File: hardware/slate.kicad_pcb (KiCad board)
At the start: 4 copper layers, 2 parts, among them U1 A33, U2 H5TQ4G63EFR

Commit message: Update
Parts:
- added R1: 240, Resistor_SMD:R_0201_0603Metric, B.Cu at (156.8, 103.5)
- added R2: 240, Resistor_SMD:R_0201_0603Metric, F.Cu at (171.4, 93.7)
- added U3: H5TQ4G63EFR, Package_BGA:FBGA-96_7.5x13mm_Layout9x16_P0.8mm, F.Cu at (159.1, 119.4)
- U2: moved to B.Cu
- moved U1 17.7 mm to (137.1, 101.5)
- moved U2 12.1 mm to (169.0, 119.5), turned to 180 degrees
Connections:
- U1 pad H5: VCC-DRAM -> +1V5
- U1 pad H6: VCC-DRAM -> +1V5
- U1 pad J5: VCC-DRAM -> +1V5
- U1 pad J6: VCC-DRAM -> +1V5
- U1 pad K5: VCC-DRAM -> +1V5
- U1 pad L5: VCC-DRAM -> +1V5
- U2 pad A1: VDDQ -> +1V5
- U2 pad A8: VDDQ -> +1V5
- U2 pad B2: VDD -> +1V5
- U2 pad C1: VDDQ -> +1V5
- U2 pad C9: VDDQ -> +1V5
- U2 pad D2: VDDQ -> +1V5
- U2 pad D9: VDD -> +1V5
- U2 pad E9: VDDQ -> +1V5
- U2 pad F1: VDDQ -> +1V5
- U2 pad G7: VDD -> +1V5
- U2 pad H2: VDDQ -> +1V5
- U2 pad H9: VDDQ -> +1V5
- U2 pad J3: unconnected-(U2-~{RAS}-PadJ3) -> /DDR3 RAM/~{RAS}
- U2 pad K2: VDD -> +1V5
- U2 pad K3: unconnected-(U2-~{CAS}-PadK3) -> /DDR3 RAM/~{CAS}
- U2 pad K8: VDD -> +1V5
- U2 pad L2: unconnected-(U2-~{CS}-PadL2) -> /DDR3 RAM/~{DDRCS}
- U2 pad L3: unconnected-(U2-~{WE}-PadL3) -> /DDR3 RAM/~{WE}
- U2 pad L7: unconnected-(U2-A10/AP-PadL7) -> /DDR3 RAM/A10
- U2 pad L8: unconnected-(U2-ZQ-PadL8) -> Net-(U2-ZQ)
- U2 pad M2: unconnected-(U2-BA0-PadM2) -> /DDR3 RAM/BA0
- U2 pad M3: unconnected-(U2-BA2-PadM3) -> /DDR3 RAM/BA2
- U2 pad N1: VDD -> +1V5
- U2 pad N2: unconnected-(U2-A3-PadN2) -> /DDR3 RAM/A3
- U2 pad N3: unconnected-(U2-A0-PadN3) -> /DDR3 RAM/A0
- U2 pad N7: unconnected-(U2-A12/~{BC}-PadN7) -> /DDR3 RAM/A12
- U2 pad N8: unconnected-(U2-BA1-PadN8) -> /DDR3 RAM/BA1
- U2 pad N9: VDD -> +1V5
- U2 pad P2: unconnected-(U2-A5-PadP2) -> /DDR3 RAM/A5
- U2 pad P3: unconnected-(U2-A2-PadP3) -> /DDR3 RAM/A2
- U2 pad P7: unconnected-(U2-A1-PadP7) -> /DDR3 RAM/A1
- U2 pad P8: unconnected-(U2-A4-PadP8) -> /DDR3 RAM/A4
- U2 pad R1: VDD -> +1V5
- U2 pad R2: unconnected-(U2-A7-PadR2) -> /DDR3 RAM/A7
- U2 pad R3: unconnected-(U2-A9-PadR3) -> /DDR3 RAM/A9
- U2 pad R7: unconnected-(U2-A11-PadR7) -> /DDR3 RAM/A11
- U2 pad R8: unconnected-(U2-A6-PadR8) -> /DDR3 RAM/A6
- U2 pad R9: VDD -> +1V5
- U2 pad T2: unconnected-(U2-~{RESET}-PadT2) -> /DDR3 RAM/~{DDRRST}
- U2 pad T3: unconnected-(U2-A13-PadT3) -> /DDR3 RAM/A13
- U2 pad T7: unconnected-(U2-A14-PadT7) -> /DDR3 RAM/A14
- U2 pad T8: unconnected-(U2-A8-PadT8) -> /DDR3 RAM/A8

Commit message: Update
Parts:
- added C1: 100n, Capacitor_SMD:C_0201_0603Metric, F.Cu at (141.3, 43.2)
- added C10: 100n, Capacitor_SMD:C_0201_0603Metric, F.Cu at (143.7, 45.0)
- added C11: 100n, Capacitor_SMD:C_0201_0603Metric, F.Cu at (143.7, 46.7)
- added C12: 100n, Capacitor_SMD:C_0201_0603Metric, F.Cu at (143.7, 48.5)
- added C13: 100n, Capacitor_SMD:C_0201_0603Metric, F.Cu at (143.7, 50.2)
- added C14: 100n, Capacitor_SMD:C_0201_0603Metric, F.Cu at (143.7, 52.0)
- added C15: 100n, Capacitor_SMD:C_0201_0603Metric, F.Cu at (143.7, 53.7)
- added C16: 100n, Capacitor_SMD:C_0201_0603Metric, F.Cu at (143.7, 55.5)
- added C17: 100n, Capacitor_SMD:C_0201_0603Metric, F.Cu at (146.2, 43.2)
- added C18: 100n, Capacitor_SMD:C_0201_0603Metric, F.Cu at (146.2, 45.0)
- added C19: 100n, Capacitor_SMD:C_0201_0603Metric, F.Cu at (146.2, 46.7)
- added C2: 100n, Capacitor_SMD:C_0201_0603Metric, F.Cu at (141.3, 45.0)
- added C20: 100n, Capacitor_SMD:C_0201_0603Metric, F.Cu at (146.2, 48.5)
- added C21: 100n, Capacitor_SMD:C_0201_0603Metric, F.Cu at (146.2, 50.2)
- added C22: 100n, Capacitor_SMD:C_0201_0603Metric, F.Cu at (146.2, 52.0)
- added C23: 100n, Capacitor_SMD:C_0201_0603Metric, F.Cu at (146.2, 53.7)
- added C24: 100n, Capacitor_SMD:C_0201_0603Metric, F.Cu at (146.2, 55.5)
- added C25: 100n, Capacitor_SMD:C_0201_0603Metric, F.Cu at (126.5, 98.8)
- added C26: 100n, Capacitor_SMD:C_0201_0603Metric, F.Cu at (126.5, 100.5)
- added C3: 100n, Capacitor_SMD:C_0201_0603Metric, F.Cu at (141.3, 46.7)
- added C4: 100n, Capacitor_SMD:C_0201_0603Metric, F.Cu at (141.3, 48.5)
- added C5: 100n, Capacitor_SMD:C_0201_0603Metric, F.Cu at (141.3, 50.2)
- added C6: 100n, Capacitor_SMD:C_0201_0603Metric, F.Cu at (141.3, 52.0)
- added C7: 100n, Capacitor_SMD:C_0201_0603Metric, F.Cu at (141.3, 53.7)
- added C8: 100n, Capacitor_SMD:C_0201_0603Metric, F.Cu at (141.3, 55.5)
- added C9: 100n, Capacitor_SMD:C_0201_0603Metric, F.Cu at (143.7, 43.2)
- added R10: 1k, Resistor_SMD:R_0201_0603Metric, F.Cu at (126.5, 104.0)
- added R3: 1k, Resistor_SMD:R_0201_0603Metric, F.Cu at (148.6, 45.0)
- added R4: 240, Resistor_SMD:R_0201_0603Metric, F.Cu at (131.3, 35.9)
- added R5: 2k, Resistor_SMD:R_0201_0603Metric, F.Cu at (148.6, 48.5)
- added R6: 240, Resistor_SMD:R_0201_0603Metric, F.Cu at (135.7, 35.9)
- added R7: 240, Resistor_SMD:R_0201_0603Metric, F.Cu at (131.3, 37.7)
- added R8: 240, Resistor_SMD:R_0201_0603Metric, F.Cu at (131.3, 39.4)
- added R9: 1k, Resistor_SMD:R_0201_0603Metric, F.Cu at (126.5, 102.3)
- R2: value 240 -> 1k
- U2: value H5TQ4G63EFR -> H5TQ4G83EFR; footprint Package_BGA:FBGA-96_7.5x13mm_Layout9x16_P0.8mm -> Package_BGA:FBGA-78_7.5x11mm_Layout2x3x13_P0.8mm; moved to F.Cu
- U3: value H5TQ4G63EFR -> H5TQ4G83EFR; footprint Package_BGA:FBGA-96_7.5x13mm_Layout9x16_P0.8mm -> Package_BGA:FBGA-78_7.5x11mm_Layout2x3x13_P0.8mm
- moved U2 83.7 mm to (119.6, 51.9), turned to 0 degrees
- moved U3 72.5 mm to (132.6, 51.9)
- moved R1 67.3 mm to (137.8, 38.9)
- moved R2 55.4 mm to (148.6, 43.2)
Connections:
- R1 pad 1: Net-(U2-ZQ) -> Net-(U2-ZQ0)
- R2 pad 1: Net-(U3-ZQ) -> +1V5
- R2 pad 2: GND -> Net-(U2-VREFCA)
- U1 pad A1: unconnected-(U1B-DA6-PadA1) -> /A33/A6
- U1 pad B1: unconnected-(U1B-DA8-PadB1) -> /A33/A8
- U1 pad C1: unconnected-(U1B-DA14-PadC1) -> /A33/A14
- U1 pad C2: unconnected-(U1B-DA11-PadC2) -> /A33/A11
- U1 pad D1: unconnected-(U1B-DA1-PadD1) -> /A33/A1
- U1 pad D2: unconnected-(U1B-DA4-PadD2) -> /A33/A4
- U1 pad E1: unconnected-(U1B-DA12-PadE1) -> /A33/A12
- U1 pad E2: unconnected-(U1B-DA10-PadE2) -> /A33/A10
- U1 pad E3: unconnected-(U1B-DA15-PadE3) -> /A33/A15
- U1 pad E4: unconnected-(U1B-DA0-PadE4) -> /A33/A0
- U1 pad F1: unconnected-(U1B-DA5-PadF1) -> /A33/A5
- U1 pad F2: unconnected-(U1B-DA2-PadF2) -> /A33/A2
- U1 pad F3: unconnected-(U1B-DA13-PadF3) -> /A33/A13
- U1 pad F4: unconnected-(U1B-DA9-PadF4) -> /A33/A9
- U1 pad G1: unconnected-(U1B-DCK-PadG1) -> /A33/CLK+
- U1 pad G2: unconnected-(U1B-DCKB-PadG2) -> /A33/CLK-
- U1 pad G3: unconnected-(U1B-DRST-PadG3) -> /A33/~{RESET}
- U1 pad G4: unconnected-(U1B-DA7-PadG4) -> /A33/A7
- U1 pad H3: unconnected-(U1B-DA3-PadH3) -> /A33/A3
- U1 pad H4: unconnected-(U1B-DBA2-PadH4) -> /A33/BA2
- U1 pad J3: unconnected-(U1B-DBA0-PadJ3) -> /A33/BA0
- U1 pad J4: unconnected-(U1B-DCKE-PadJ4) -> /A33/CKE0
- U1 pad K1: unconnected-(U1B-DQS0B-PadK1) -> /A33/DQS0-
- U1 pad K2: unconnected-(U1B-DQS0-PadK2) -> /A33/DQS0+
- U1 pad K3: unconnected-(U1B-DWE-PadK3) -> /A33/~{WE}
- U1 pad K4: unconnected-(U1B-DBA1-PadK4) -> /A33/BA1
- U1 pad L3: unconnected-(U1B-DODT-PadL3) -> /A33/ODT0
- U1 pad L4: unconnected-(U1B-DRAS-PadL4) -> /A33/~{RAS}
- U1 pad L7: unconnected-(U1B-DODT1-PadL7) -> /A33/ODT1
- U1 pad M3: unconnected-(U1B-DCAS-PadM3) -> /A33/~{CAS}
- U1 pad M4: unconnected-(U1A-DVREF-PadM4) -> Net-(U1B-DVREF)
- U1 pad N2: unconnected-(U1B-DQM0-PadN2) -> /A33/DQM0
- U1 pad N3: unconnected-(U1B-DCS-PadN3) -> /A33/~{CS0}
- U1 pad N5: unconnected-(U1B-DCS1-PadN5) -> /A33/~{CS1}
- U1 pad N7: unconnected-(U1B-DCKE1-PadN7) -> /A33/CKE1
- U1 pad R1: unconnected-(U1B-DQS1-PadR1) -> /A33/DQS1+
- U1 pad R3: unconnected-(U1B-DZQ-PadR3) -> Net-(U1B-DZQ)
- U1 pad T1: unconnected-(U1B-DQS1B-PadT1) -> /A33/DQS1-
- U1 pad T3: unconnected-(U1B-DQM1-PadT3) -> /A33/DQM1
- U2 pad A1: +1V5 -> GND
- U2 pad A2: unconnected-(U2-DQU5-PadA2) -> +1V5
- U2 pad A8: +1V5 -> GND
- U2 pad A9: GND -> +1V5
- U2 pad B2: +1V5 -> GND
- U2 pad B3: GND -> unconnected-(U2-DQ0-PadB3)
- U2 pad B7: unconnected-(U2-~{DQSU}-PadB7) -> /A33/DQM0
- U2 pad B8: unconnected-(U2-DQU6-PadB8) -> GND
- U2 pad B9: GND -> +1V5
- U2 pad C3: unconnected-(U2-DQU1-PadC3) -> /A33/DQS0+
- U2 pad C9: +1V5 -> GND
- U2 pad D2: +1V5 -> unconnected-(U2-DQ6-PadD2)
- U2 pad D3: unconnected-(U2-DMU-PadD3) -> /A33/DQS0-
- U2 pad D7: unconnected-(U2-DQU0-PadD7) -> +1V5
- U2 pad D9: +1V5 -> GND
- U2 pad E1: GND -> Net-(U2-VREFCA)
- U2 pad E2: GND -> +1V5
- U2 pad E8: GND -> unconnected-(U2-DQ5-PadE8)
- U2 pad F1: +1V5 -> /A33/ODT1
- U2 pad F2: unconnected-(U2-DQL2-PadF2) -> GND
- U2 pad F3: unconnected-(U2-DQSL-PadF3) -> /A33/~{RAS}
- U2 pad F7: unconnected-(U2-DQL1-PadF7) -> /A33/CLK+
- U2 pad F8: unconnected-(U2-DQL3-PadF8) -> GND
- U2 pad F9: GND -> /A33/CKE1
- U2 pad G1: GND -> /A33/ODT0
- U2 pad G2: unconnected-(U2-DQL6-PadG2) -> +1V5
- U2 pad G3: unconnected-(U2-~{DQSL}-PadG3) -> /A33/~{CAS}
- U2 pad G7: +1V5 -> /A33/CLK-
- U2 pad G8: GND -> +1V5
- U2 pad G9: GND -> /A33/CKE0
- U2 pad H1: unconnected-(U2-VREFDQ-PadH1) -> /A33/~{CS1}
- U2 pad H2: +1V5 -> /A33/~{CS0}
- U2 pad H3: unconnected-(U2-DQL4-PadH3) -> /A33/~{WE}
- U2 pad H7: unconnected-(U2-DQL7-PadH7) -> /A33/A10
- U2 pad H8: unconnected-(U2-DQL5-PadH8) -> Net-(U2-ZQ0)
- U2 pad H9: +1V5 -> Net-(U2-ZQ1/NC)
- U2 pad J1: unconnected-(U2-NC-PadJ1) -> GND
- U2 pad J2: GND -> /A33/BA0
- U2 pad J3: /DDR3 RAM/~{RAS} -> /A33/BA2
- U2 pad J7: unconnected-(U2-CK-PadJ7) -> /A33/A15
- U2 pad J8: GND -> Net-(U2-VREFCA)
- U2 pad J9: unconnected-(U2-NC-PadJ9) -> GND
- U2 pad K1: unconnected-(U2-ODT-PadK1) -> +1V5
- U2 pad K2: +1V5 -> /A33/A3
- U2 pad K3: /DDR3 RAM/~{CAS} -> /A33/A0
- U2 pad K7: unconnected-(U2-~{CK}-PadK7) -> /A33/A12
- U2 pad K8: +1V5 -> /A33/BA1
- U2 pad K9: unconnected-(U2-CKE-PadK9) -> +1V5
- U2 pad L1: unconnected-(U2-NC-PadL1) -> GND
- U2 pad L2: /DDR3 RAM/~{DDRCS} -> /A33/A5
- U2 pad L3: /DDR3 RAM/~{WE} -> /A33/A2
- U2 pad L7: /DDR3 RAM/A10 -> /A33/A1
- U2 pad L8: Net-(U2-ZQ) -> /A33/A4
- U2 pad L9: unconnected-(U2-NC-PadL9) -> GND
- U2 pad M1: GND -> +1V5
- U2 pad M2: /DDR3 RAM/BA0 -> /A33/A7
- U2 pad M3: /DDR3 RAM/BA2 -> /A33/A9
- U2 pad M7: unconnected-(U2-NC-PadM7) -> /A33/A11
- U2 pad M8: unconnected-(U2-VREFCA-PadM8) -> /A33/A6
- U2 pad M9: GND -> +1V5
- U2 pad N1: +1V5 -> GND
- U2 pad N2: /DDR3 RAM/A3 -> /A33/~{RESET}
- U2 pad N3: /DDR3 RAM/A0 -> /A33/A13
- U2 pad N7: /DDR3 RAM/A12 -> /A33/A14
- U2 pad N8: /DDR3 RAM/BA1 -> /A33/A8
- U2 pad N9: +1V5 -> GND
- U3 pad A1: +1V5 -> GND
- U3 pad A2: unconnected-(U3-DQU5-PadA2) -> +1V5
- U3 pad A8: +1V5 -> GND
- U3 pad A9: GND -> +1V5
- U3 pad B2: +1V5 -> GND
- U3 pad B3: GND -> unconnected-(U3-DQ0-PadB3)
- U3 pad B7: unconnected-(U3-~{DQSU}-PadB7) -> /A33/DQM1
- U3 pad B8: unconnected-(U3-DQU6-PadB8) -> GND
- U3 pad B9: GND -> +1V5
- U3 pad C3: unconnected-(U3-DQU1-PadC3) -> /A33/DQS1+
- U3 pad C9: +1V5 -> GND
- U3 pad D2: +1V5 -> unconnected-(U3-DQ6-PadD2)
- U3 pad D3: unconnected-(U3-DMU-PadD3) -> /A33/DQS1-
- U3 pad D7: unconnected-(U3-DQU0-PadD7) -> +1V5
- U3 pad D9: +1V5 -> GND
- U3 pad E1: GND -> Net-(U2-VREFCA)
- U3 pad E2: GND -> +1V5
- U3 pad E8: GND -> unconnected-(U3-DQ5-PadE8)
- U3 pad F1: +1V5 -> /A33/ODT1
- U3 pad F2: unconnected-(U3-DQL2-PadF2) -> GND
- U3 pad F3: unconnected-(U3-DQSL-PadF3) -> /A33/~{RAS}
- U3 pad F7: unconnected-(U3-DQL1-PadF7) -> /A33/CLK+
- U3 pad F8: unconnected-(U3-DQL3-PadF8) -> GND
- U3 pad F9: GND -> /A33/CKE1
- U3 pad G1: GND -> /A33/ODT0
- U3 pad G2: unconnected-(U3-DQL6-PadG2) -> +1V5
- U3 pad G3: unconnected-(U3-~{DQSL}-PadG3) -> /A33/~{CAS}
- U3 pad G7: +1V5 -> /A33/CLK-
- U3 pad G8: GND -> +1V5
- U3 pad G9: GND -> /A33/CKE0
- U3 pad H1: unconnected-(U3-VREFDQ-PadH1) -> /A33/~{CS1}
- U3 pad H2: +1V5 -> /A33/~{CS0}
- U3 pad H3: unconnected-(U3-DQL4-PadH3) -> /A33/~{WE}
- U3 pad H7: unconnected-(U3-DQL7-PadH7) -> /A33/A10
- U3 pad H8: unconnected-(U3-DQL5-PadH8) -> Net-(U3-ZQ0)
- U3 pad H9: +1V5 -> Net-(U3-ZQ1/NC)
- U3 pad J1: unconnected-(U3-NC-PadJ1) -> GND
- U3 pad J2: GND -> /A33/BA0
- U3 pad J3: /DDR3 RAM/~{RAS} -> /A33/BA2
- U3 pad J7: unconnected-(U3-CK-PadJ7) -> /A33/A15
- U3 pad J8: GND -> Net-(U2-VREFCA)
- U3 pad J9: unconnected-(U3-NC-PadJ9) -> GND
- U3 pad K1: unconnected-(U3-ODT-PadK1) -> +1V5
- U3 pad K2: +1V5 -> /A33/A3
- U3 pad K3: /DDR3 RAM/~{CAS} -> /A33/A0
- U3 pad K7: unconnected-(U3-~{CK}-PadK7) -> /A33/A12
- U3 pad K8: +1V5 -> /A33/BA1
- U3 pad K9: unconnected-(U3-CKE-PadK9) -> +1V5
- U3 pad L1: unconnected-(U3-NC-PadL1) -> GND
- U3 pad L2: /DDR3 RAM/~{DDRCS} -> /A33/A5
- U3 pad L3: /DDR3 RAM/~{WE} -> /A33/A2
- U3 pad L7: /DDR3 RAM/A10 -> /A33/A1
- U3 pad L8: Net-(U3-ZQ) -> /A33/A4
- U3 pad L9: unconnected-(U3-NC-PadL9) -> GND
- U3 pad M1: GND -> +1V5
- U3 pad M2: /DDR3 RAM/BA0 -> /A33/A7
- U3 pad M3: /DDR3 RAM/BA2 -> /A33/A9
- U3 pad M7: unconnected-(U3-NC-PadM7) -> /A33/A11
- U3 pad M8: unconnected-(U3-VREFCA-PadM8) -> /A33/A6
- U3 pad M9: GND -> +1V5
- U3 pad N1: +1V5 -> GND
- U3 pad N2: /DDR3 RAM/A3 -> /A33/~{RESET}
- U3 pad N3: /DDR3 RAM/A0 -> /A33/A13
- U3 pad N7: /DDR3 RAM/A12 -> /A33/A14
- U3 pad N8: /DDR3 RAM/BA1 -> /A33/A8
- U3 pad N9: +1V5 -> GND

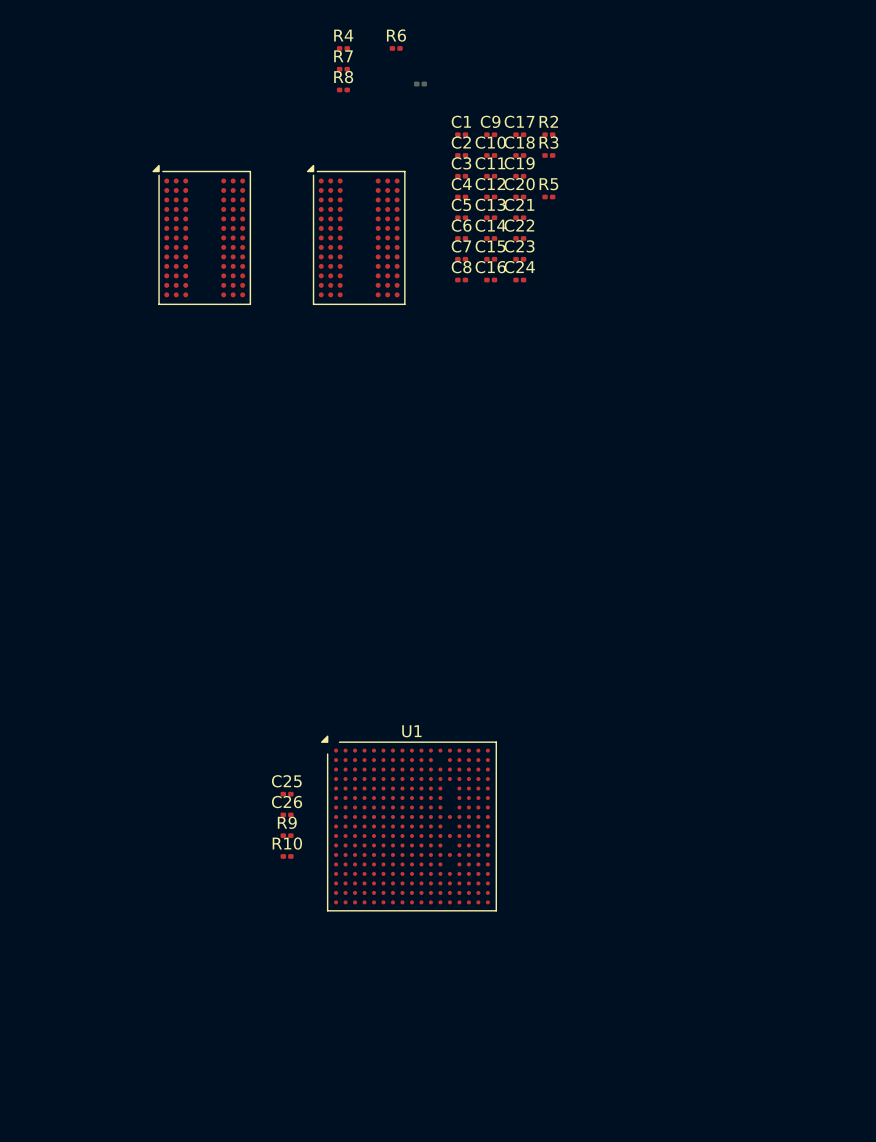
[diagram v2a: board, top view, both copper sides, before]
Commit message: Start of psu
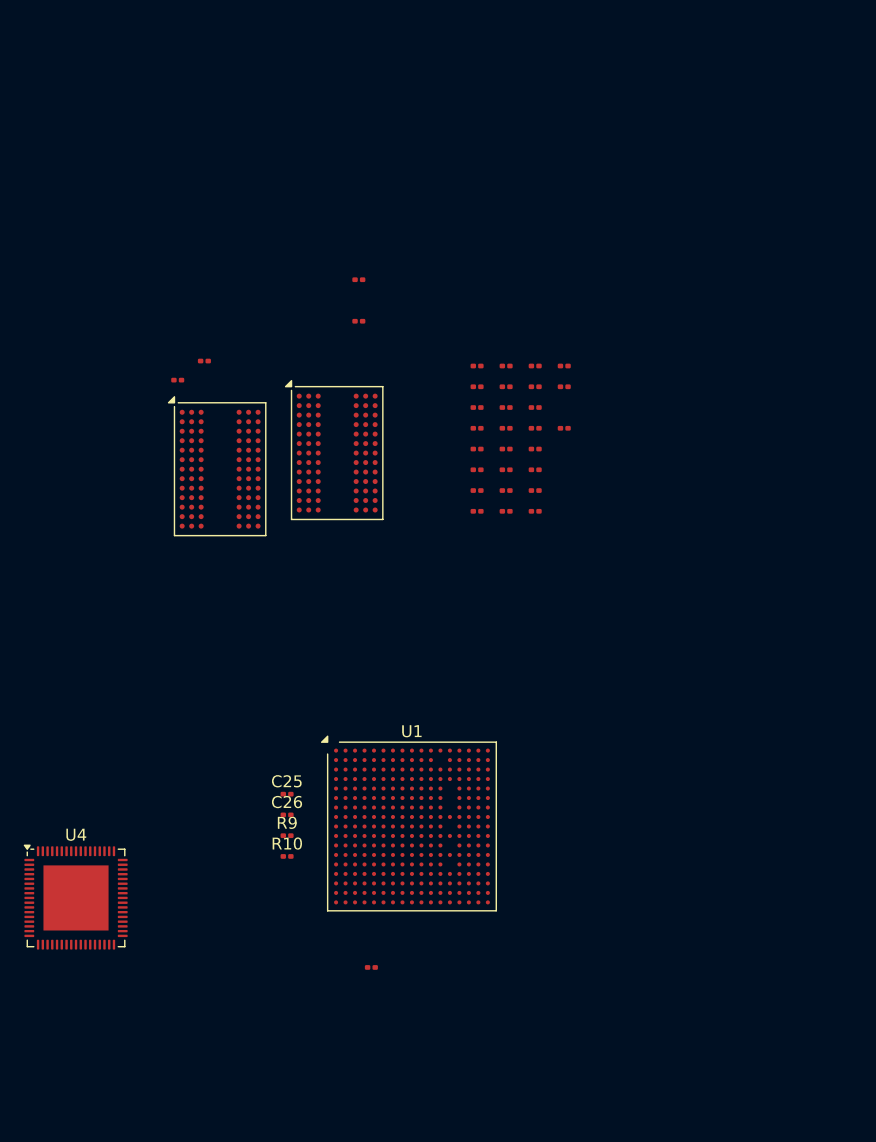
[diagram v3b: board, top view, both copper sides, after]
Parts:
- added U4: AXP223, slate-lib:QFN-68-1EP_8x8mm_P0.4mm_EP5.49x5.49mm, F.Cu at (108.8, 107.5)
- R1: moved to F.Cu
- moved R6 77.5 mm to (133.7, 113.4)
- moved R7 29.7 mm to (117.3, 63.9)
- moved R1 29.6 mm to (119.6, 62.3)
- moved U2 19.5 mm to (120.9, 71.4)
- moved C1 19.5 mm to (142.6, 62.7)
- moved C17 19.5 mm to (147.5, 62.7)
- moved C18 19.5 mm to (147.5, 64.5)
- moved C19 19.5 mm to (147.5, 66.2)
- moved C2 19.5 mm to (142.6, 64.5)
- moved C20 19.5 mm to (147.5, 68.0)
- moved C21 19.5 mm to (147.5, 69.7)
- moved C22 19.5 mm to (147.5, 71.5)
- moved C23 19.5 mm to (147.5, 73.2)
- moved C24 19.5 mm to (147.5, 75.0)
- moved C3 19.5 mm to (142.6, 66.2)
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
